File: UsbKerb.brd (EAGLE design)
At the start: 100 x 80 mm, 21 parts, among them IC1 XMEGA16A4A

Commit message: board Layout complete?
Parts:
- removed U$1: 3.3TVS, usb:SOT23-6L
- added C8: 470uf, rcl:PANASONIC_G
- added U1: UA78M33CDCY, usb:SOT230P700X180-4N
- added U2: 3.3TVS, usb:SOT23-6L
- moved C6 85.1 mm to (41.1, 30.0), turned to 180 degrees
- moved C3 72.6 mm to (33.8, 24.4), turned to 90 degrees
- moved C7 72.4 mm to (22.4, 5.33), turned to 270 degrees
- moved R3 71.8 mm to (26.7, 30.5), turned to 90 degrees
- moved U$4 70.0 mm to (17.0, 9.14), turned to 180 degrees
- moved C5 64.4 mm to (15.0, 5.33), turned to 90 degrees
- moved C4 63.6 mm to (19.1, 5.33), turned to 90 degrees
- moved C2 63.1 mm to (31.2, 30.2), turned to 90 degrees
- moved C1 55.3 mm to (29.0, 24.4), turned to 90 degrees
- moved U$3 53.0 mm to (29.7, 16.0), turned to 180 degrees
- moved JP1 52.7 mm to (15.2, 36.8)
- moved JP2 47.1 mm to (29.2, 36.8)
- moved IC1 46.3 mm to (18.8, 19.1), turned to 180 degrees
- moved D- 46.0 mm to (3.81, 21.6)
- moved R5 45.8 mm to (19.3, 30.5), turned to 90 degrees
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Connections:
- removed net N$15: JP2.3
- new net +3V3: C6.+, C7.1, IC1.19, IC1.31, IC1.39, IC1.9, JP1.1, JP1.2, JP1.8, U$3.C, U1.1, U2.5
- net +5V: now also C8.+, U1.3; no longer C6.+, C7.1, IC1.19, IC1.31, IC1.39, IC1.9, JP1.1, JP1.2, JP1.8, U$1.5, U$3.C
- net GND: now also C8.-, U1.2, U1.4, U2.2; no longer U$1.2
- net N$18: now also JP2.3
- net N$2: now also U2.3; no longer U$1.3
- net N$4: now also U2.1; no longer U$1.1
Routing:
- net GND: track 0.00 -> 180.8 mm, vias 0 -> 2
- net +3V3: track 0.00 -> 135.5 mm, vias 0 -> 6
- net +5V: track 0.00 -> 110.2 mm, vias 0 -> 2
- net N$19: track 0.00 -> 48.8 mm
- net N$16: track 0.00 -> 42.5 mm
- net N$11: track 0.00 -> 37.1 mm, vias 0 -> 1
- net N$6: track 0.00 -> 33.3 mm, vias 0 -> 3
- net N$1: track 0.00 -> 32.8 mm, vias 0 -> 2
- net N$5: track 0.00 -> 31.8 mm, vias 0 -> 2
- net N$12: track 0.00 -> 27.6 mm, vias 0 -> 1
- net N$17: track 0.00 -> 24.0 mm, vias 0 -> 1
- net N$18: track 0.00 -> 23.8 mm, vias 0 -> 1
- net N$9: track 0.00 -> 15.4 mm
- net N$2: track 0.00 -> 13.9 mm
- net N$8: track 0.00 -> 12.6 mm
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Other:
- board size 100 x 80 mm -> 51.4 x 44.4 mm

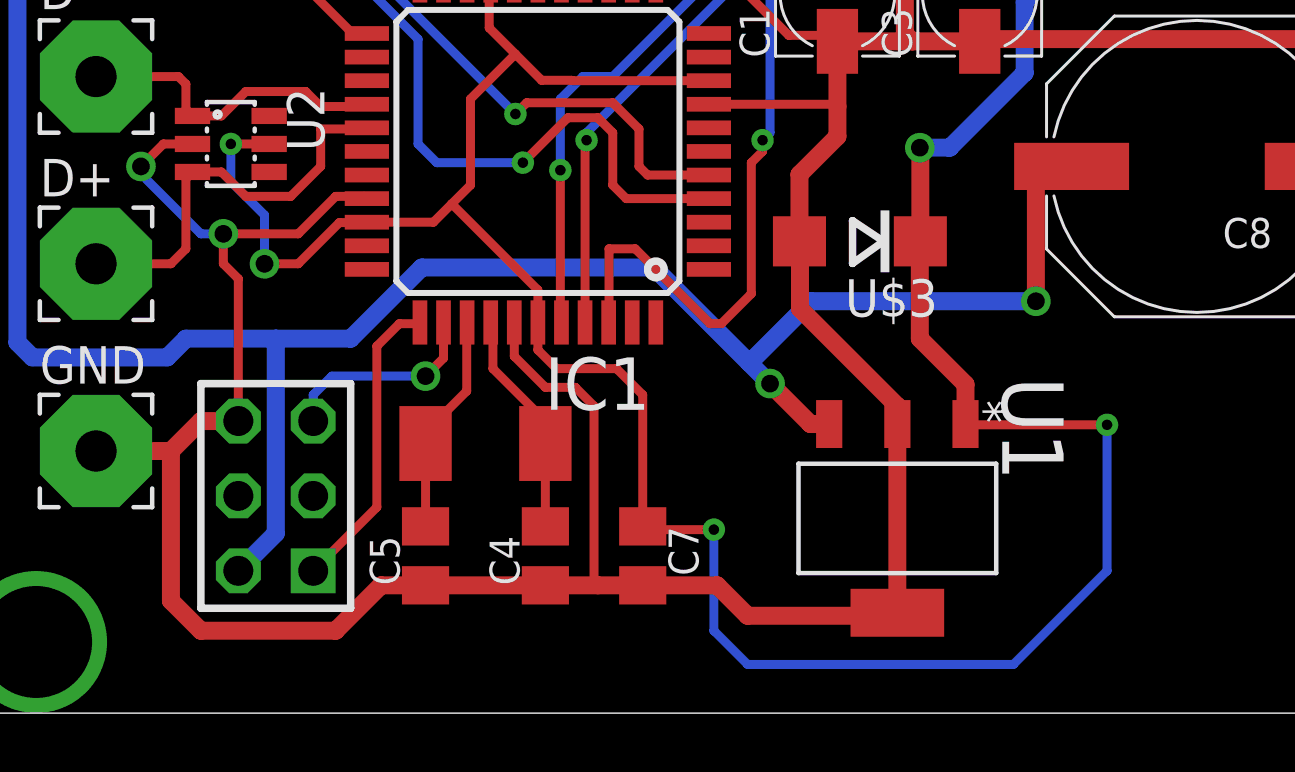
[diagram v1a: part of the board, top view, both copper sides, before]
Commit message: Corrected board layout for voltage and regulator footprint
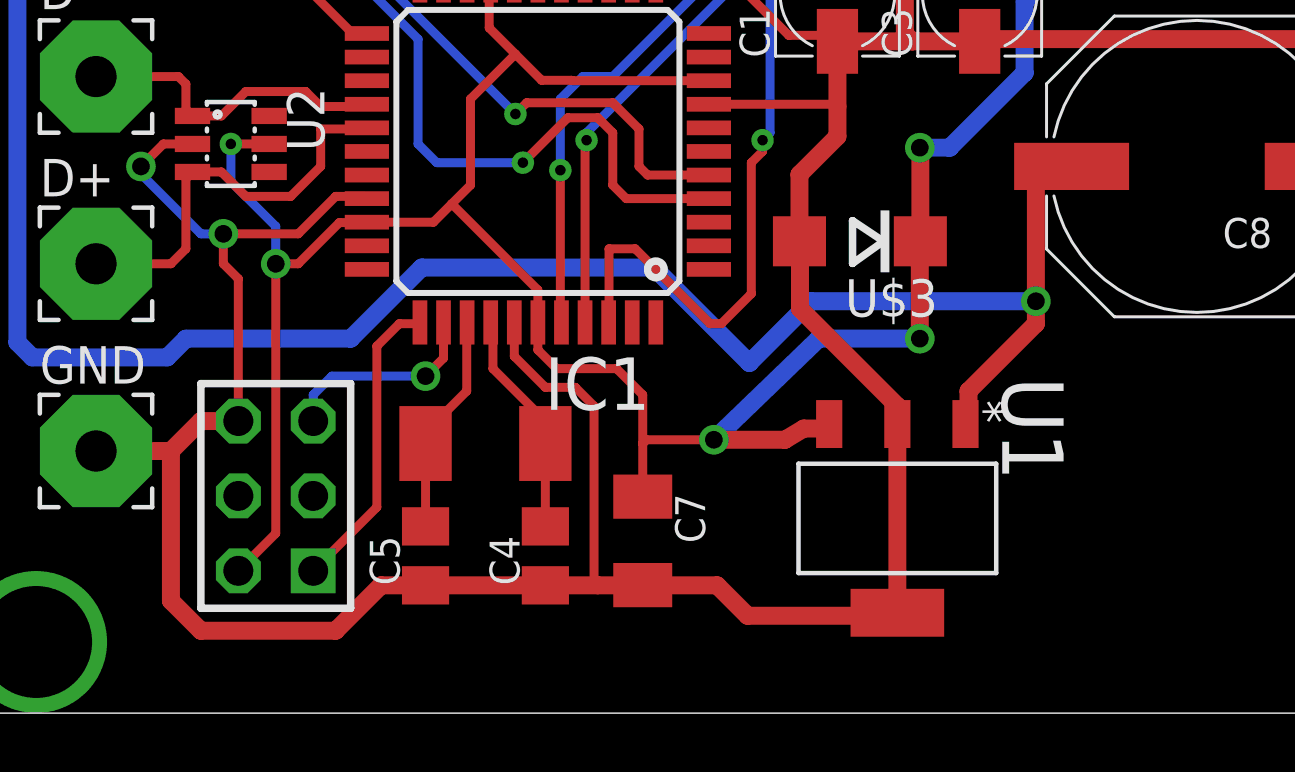
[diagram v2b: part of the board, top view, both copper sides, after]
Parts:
- C7: device rcl:C0805K -> resistor:C1206K
- moved C7 0.51 mm to (22.4, 5.84)
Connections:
- net +3V3: now also U$2.2, U1.3; no longer U1.1
- net +5V: now also U1.1; no longer U$2.2, U1.3
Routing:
- net +3V3: track 135.5 -> 125.8 mm
- net +5V: track 110.2 -> 103.4 mm, vias 2 -> 1

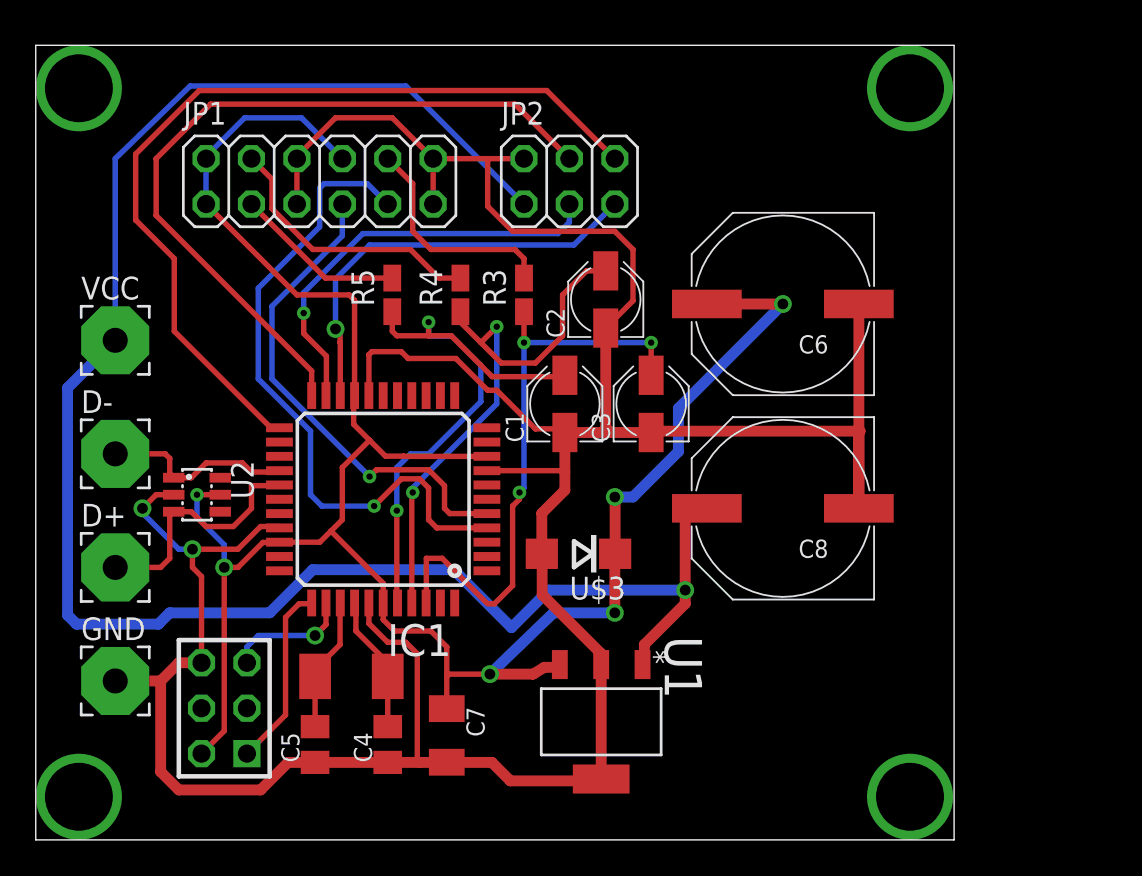
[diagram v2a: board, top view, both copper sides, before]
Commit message: Swapped USB Pads for USB Mini connector
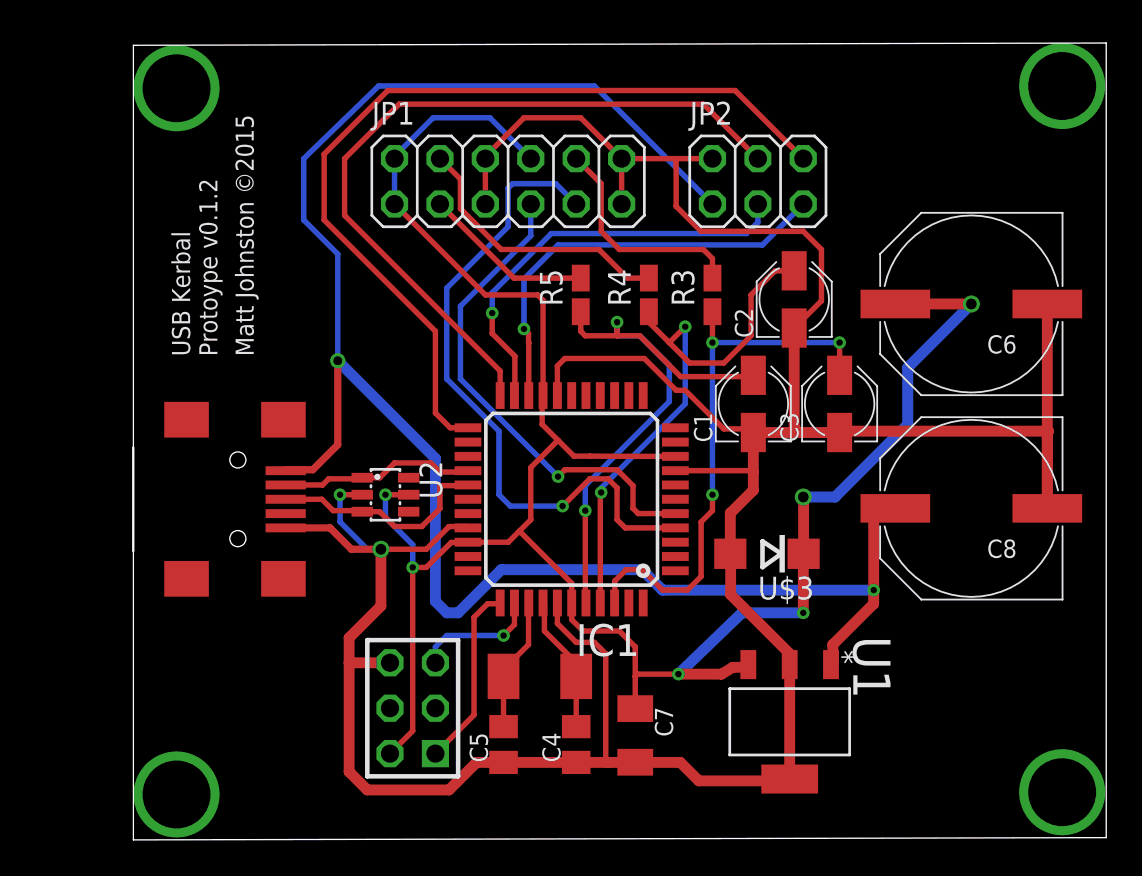
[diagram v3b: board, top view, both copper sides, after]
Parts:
- removed D+, D-, GND, VCC: (no value), wirepad:3,81/1,4
- added U$1: USB-MINI, usb:USB-MINI
- moved C3 10.5 mm to (44.3, 24.4)
- moved U1 10.5 mm to (41.5, 6.60)
- moved C1 10.5 mm to (39.5, 24.4)
- moved C2 10.5 mm to (41.8, 30.2)
- moved C4 10.5 mm to (29.6, 5.33)
- moved C5 10.5 mm to (25.5, 5.33)
- moved C7 10.5 mm to (32.9, 5.84)
- moved IC1 10.5 mm to (29.3, 19.1)
- moved R4 10.5 mm to (33.7, 30.5)
- moved R5 10.5 mm to (29.8, 30.5)
- moved U$3 10.5 mm to (40.3, 16.0)
- moved U$4 10.5 mm to (27.6, 9.14)
- moved JP1 10.5 mm to (25.8, 36.8)
- moved U$2 10.5 mm to (20.4, 7.37)
- moved U2 10.5 mm to (18.9, 19.3)
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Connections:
- net +5V: now also U$1.VBUS; no longer VCC.1
- net GND: now also U$1.GND; no longer GND.1
- net N$2: now also U$1.D+; no longer D+.1
- net N$4: now also U$1.D-; no longer D-.1
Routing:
- net GND: track 180.8 -> 184.3 mm
- net +3V3: track 125.8 -> 122.7 mm
- net +5V: track 103.4 -> 100.5 mm, vias 1 -> 2
- net N$6: track 33.3 -> 31.1 mm
- net N$2: track 13.9 -> 12.5 mm
- net N$19: track 48.8 -> 49.6 mm
- net N$1: track 32.8 -> 32.2 mm
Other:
- board size 51.4 x 44.4 mm -> 54.4 x 44.6 mm
- board text added: "Matt Johnston ©2015"
- board text added: "USB Kerbal Protoype v0.1.2"
